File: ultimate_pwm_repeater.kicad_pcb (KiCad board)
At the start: 2 copper layers, 50.5 x 43 mm, 21 parts, among them J1 POWER, J2 SIGNAL, Q1 IRF3205, Q2 IRF3205, Q3 IRF3205, Q4 IRF3205

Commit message: added mounting holes
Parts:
- added LH: MountingHole_2.5mm_Pad, MountingHole:MountingHole_2.5mm_Pad, F.Cu at (41.5, 84.5)
- added RH: MountingHole_2.5mm_Pad, MountingHole:MountingHole_2.5mm_Pad, F.Cu at (86.0, 84.5)
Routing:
- removed copper zone on F.Cu, net GND
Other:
- board size 50.5 x 43 mm -> 50.5 x 48.5 mm
- board text added: "12-24V@20A PWM Repeater V0.3 by Hex of the River and the Sparks me@hex128.io"
- board text removed: "12-24V@20A PWM Repeater V0.2 by Hex of the River and the Sparks me@hex128.io"
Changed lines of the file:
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@@
 		(title "PWM Repeater")
 		(date "2025-04-30")
-		(rev "0.2")
+		(rev "0.3")
 		(company "Hex of the River and the Sparks")
 	)
@@
 		)
 	)
+	(footprint "MountingHole:MountingHole_2.5mm_Pad"
+		(layer "F.Cu")
+		(at 86 84.5)
+		(descr "Mounting Hole 2.5mm")
+		(tags "mounting hole 2.5mm")
+		(property "Reference" "RH"
+			(at 0 -3.5 0)
+			(layer "F.SilkS")
+			(hide yes)
+			(effects
+				(font
+					(size 1 1)
+					(thickness 0.15)
+				)
+			)
+		)
+		(property "Value" "MountingHole_2.5mm_Pad"
+			(at 0 3.5 0)
+			(layer "F.Fab")
+			(effects
+				(font
+					(size 1 1)
+					(thickness 0.15)
+				)
+			)
+		)
+		(property "Datasheet" ""
+			(at 0 0 0)
+			(unlocked yes)
+			(layer "F.Fab")
+			(hide yes)
+			(effects
+				(font
+					(size 1.27 1.27)
+					(thickness 0.15)
+				)
+			)
+		)
+		(property "Description" ""
+			(at 0 0 0)
+			(unlocked yes)
+			(layer "F.Fab")
+			(hide yes)
+			(effects
+				(font
+					(size 1.27 1.27)
+					(thickness 0.15)
+				)
+			)
+		)
+		(attr exclude_from_pos_files exclude_from_bom)
+		(fp_circle
+			(center 0 0)
+			(end 2.5 0)
+			(stroke
+				(width 0.15)
+				(type solid)
+			)
+			(fill no)
+			(layer "Cmts.User")
+		)
+		(fp_circle
+			(center 0 0)
+			(end 2.75 0)
+			(stroke
+				(width 0.05)
+				(type solid)
+			)
+			(fill no)
+			(layer "F.CrtYd")
+		)
+		(fp_text user "${REFERENCE}"
+			(at 0 0 0)
+			(layer "F.Fab")
+			(effects
+				(font
+					(size 1 1)
+					(thickness 0.15)
+				)
+			)
+		)
+		(pad "1" thru_hole circle
+			(at 0 0)
+			(size 5 5)
+			(drill 2.5)
+			(layers "*.Cu" "*.Mask")
+			(remove_unused_layers no)
+		)
+		(embedded_fonts no)
+	)
 	(footprint "PCM_Capacitor_THT_AKL:CP_Radial_D10.0mm_P2.50mm"
 		(layer "F.Cu")
@@
 		)
 	)
+	(footprint "MountingHole:MountingHole_2.5mm_Pad"
+		(layer "F.Cu")
+		(at 41.5 84.5)
+		(descr "Mounting Hole 2.5mm")
+		(tags "mounting hole 2.5mm")
+		(property "Reference" "LH"
+			(at 0 -3.5 0)
+			(layer "F.SilkS")
+			(hide yes)
+			(effects
+				(font
+					(size 1 1)
+					(thickness 0.15)
+				)
+			)
+		)
+		(property "Value" "MountingHole_2.5mm_Pad"
+			(at 0 3.5 0)
+			(layer "F.Fab")
+			(effects
+				(font
+					(size 1 1)
+					(thickness 0.15)
+				)
+			)
+		)
+		(property "Datasheet" ""
+			(at 0 0 0)
+			(unlocked yes)
+			(layer "F.Fab")
+			(hide yes)
+			(effects
+				(font
+					(size 1.27 1.27)
+					(thickness 0.15)
+				)
+			)
+		)
+		(property "Description" ""
+			(at 0 0 0)
+			(unlocked yes)
+			(layer "F.Fab")
+			(hide yes)
+			(effects
+				(font
+					(size 1.27 1.27)
+					(thickness 0.15)
+				)
+			)
+		)
+		(attr exclude_from_pos_files exclude_from_bom)
+		(fp_circle
+			(center 0 0)
+			(end 2.5 0)
+			(stroke
+				(width 0.15)
+				(type solid)
+			)
+			(fill no)
+			(layer "Cmts.User")
+		)
+		(fp_circle
+			(center 0 0)
+			(end 2.75 0)
+			(stroke
+				(width 0.05)
+				(type solid)
+			)
+			(fill no)
+			(layer "F.CrtYd")
+		)
+		(fp_text user "${REFERENCE}"
+			(at 0 0 0)
+			(layer "F.Fab")
+			(effects
+				(font
+					(size 1 1)
+					(thickness 0.15)
+				)
+			)
+		)
+		(pad "1" thru_hole circle
+			(at 0 0)
+			(size 5 5)
+			(drill 2.5)
+			(layers "*.Cu" "*.Mask")
+			(remove_unused_layers no)
+		)
+		(embedded_fonts no)
+	)
 	(footprint "PCM_Resistor_SMD_AKL:R_1206_3216Metric"
 		(layer "F.Cu")
@@
 	(gr_rect
 		(start 38.5 39)
-		(end 89 82)
+		(end 89 87.5)
 		(stroke
 			(width 0.05)
@@
 		)
 	)
-	(gr_text "12-24V@20A PWM Repeater V0.2\nby Hex of the River\nand the Sparks\nme@hex128.io"
+	(gr_text "12-24V@20A PWM Repeater V0.3\nby Hex of the River\nand the Sparks\nme@hex128.io"
 		(at 43.5 44.5 90)
 		(layer "F.SilkS")
@@
 			)
 		)
-	)
-	(zone
-		(net 1)
-		(net_name "GND")
-		(layer "F.Cu")
-		(hatch edge 0.5)
-		(priority 2)
-		(connect_pads yes
-			(clearance 0.5)
-		)
-		(min_thickness 0.5)
-		(filled_areas_thickness no)
-		(fill yes
-			(thermal_gap 0.5)
-			(thermal_bridge_width 0.5)
-			(smoothing chamfer)
-		)
-		(polygon
-			(pts
-				(xy 51 82) (xy 51 62.5) (xy 46.5 62.5) (xy 46.5 56.5) (xy 59 56.5) (xy 59 69) (xy 71.5 69) (xy 71.5 75)
-				(xy 44 75) (xy 44 82) (xy 88.5 82) (xy 88.5 62) (xy 88.5 39) (xy 39 39) (xy 39 82)
-			)
-		)

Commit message: re-added the top gnd fill zone (introduced in 0.3)
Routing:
- added copper zone on F.Cu, net GND
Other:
- board text added: "12-24V@20A PWM Repeater V0.4 by Hex of the River and the Sparks me@hex128.io"
- board text removed: "12-24V@20A PWM Repeater V0.3 by Hex of the River and the Sparks me@hex128.io"
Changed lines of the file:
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@@
 		(title "PWM Repeater")
 		(date "2025-04-30")
-		(rev "0.3")
+		(rev "0.4")
 		(company "Hex of the River and the Sparks")
 	)
@@
 		)
 	)
-	(gr_text "12-24V@20A PWM Repeater V0.3\nby Hex of the River\nand the Sparks\nme@hex128.io"
+	(gr_text "12-24V@20A PWM Repeater V0.4\nby Hex of the River\nand the Sparks\nme@hex128.io"
 		(at 43.5 44.5 90)
 		(layer "F.SilkS")
@@
 	)
 	(zone
+		(net 1)
+		(net_name "GND")
+		(layer "F.Cu")
+		(hatch edge 0.5)
+		(priority 2)
+		(connect_pads yes
+			(clearance 0.5)
+		)
+		(min_thickness 0.5)
+		(filled_areas_thickness no)
+		(fill yes
+			(thermal_gap 0.5)
+			(thermal_bridge_width 0.5)
+			(smoothing chamfer)
+			(radius 0.5)
+		)
+		(polygon
+			(pts
+				(xy 39.5 39) (xy 88 39) (xy 88 80.5) (xy 71.5 80.5) (xy 71.5 69) (xy 59 69) (xy 59 56.5) (xy 46.5 56.5)
+				(xy 46.5 62.5) (xy 51 62.5) (xy 51 75) (xy 72 75) (xy 72 80.5) (xy 39.5 80.5)
+			)
+		)
+	)
+	(zone
 		(net 6)
 		(net_name "+24V")
@@
 			(thermal_bridge_width 0.5)
 			(smoothing chamfer)
+			(radius 0.5)
 		)
 		(polygon
@@
 			(thermal_gap 0.5)
 			(thermal_bridge_width 0.5)
+			(smoothing chamfer)
+			(radius 0.5)
 			(island_removal_mode 1)
 			(island_area_min 10)
@@
 		(polygon
 			(pts
-				(xy 39.5 39) (xy 39.5 82) (xy 88 82) (xy 88 39)
+				(xy 39.5 39) (xy 39.5 80.5) (xy 88 80.5) (xy 88 39)
 			)
 		)

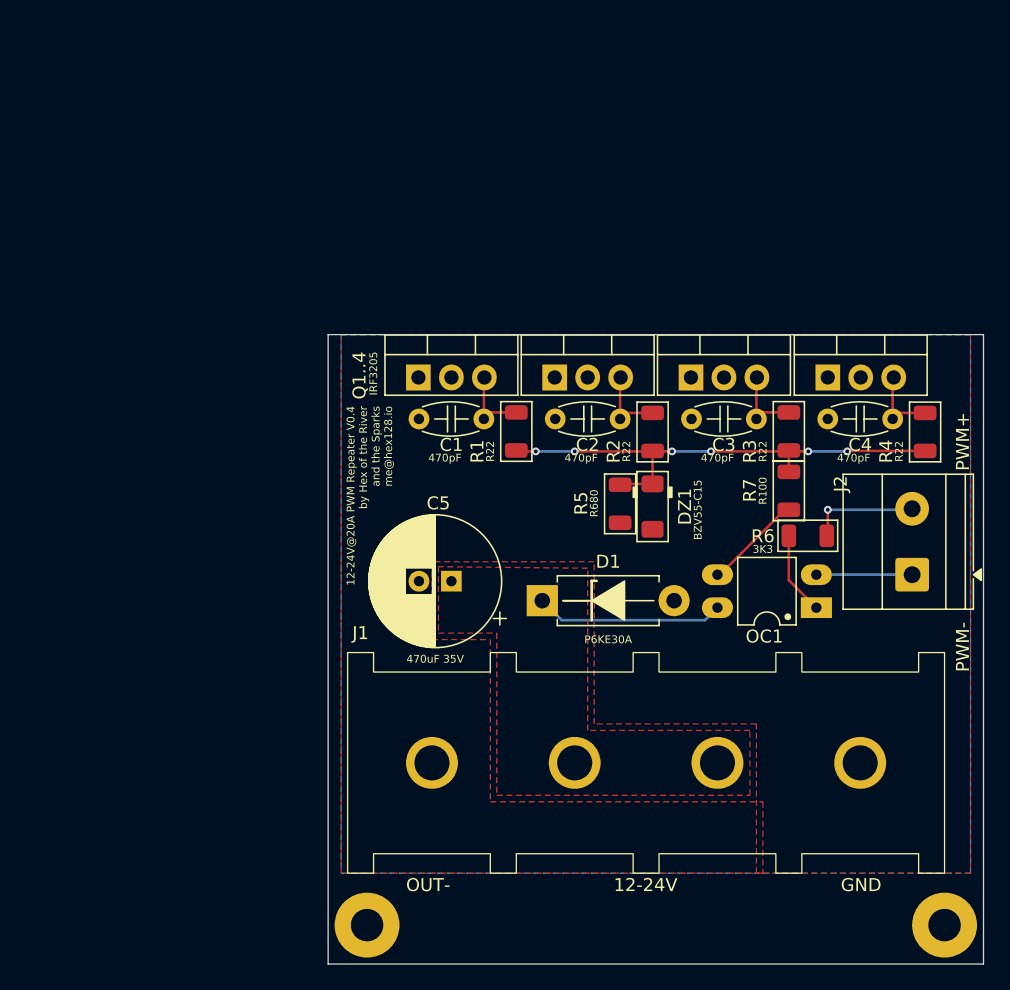
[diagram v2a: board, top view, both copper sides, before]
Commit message: fixed reverse mosfet connection, rearranged pcb
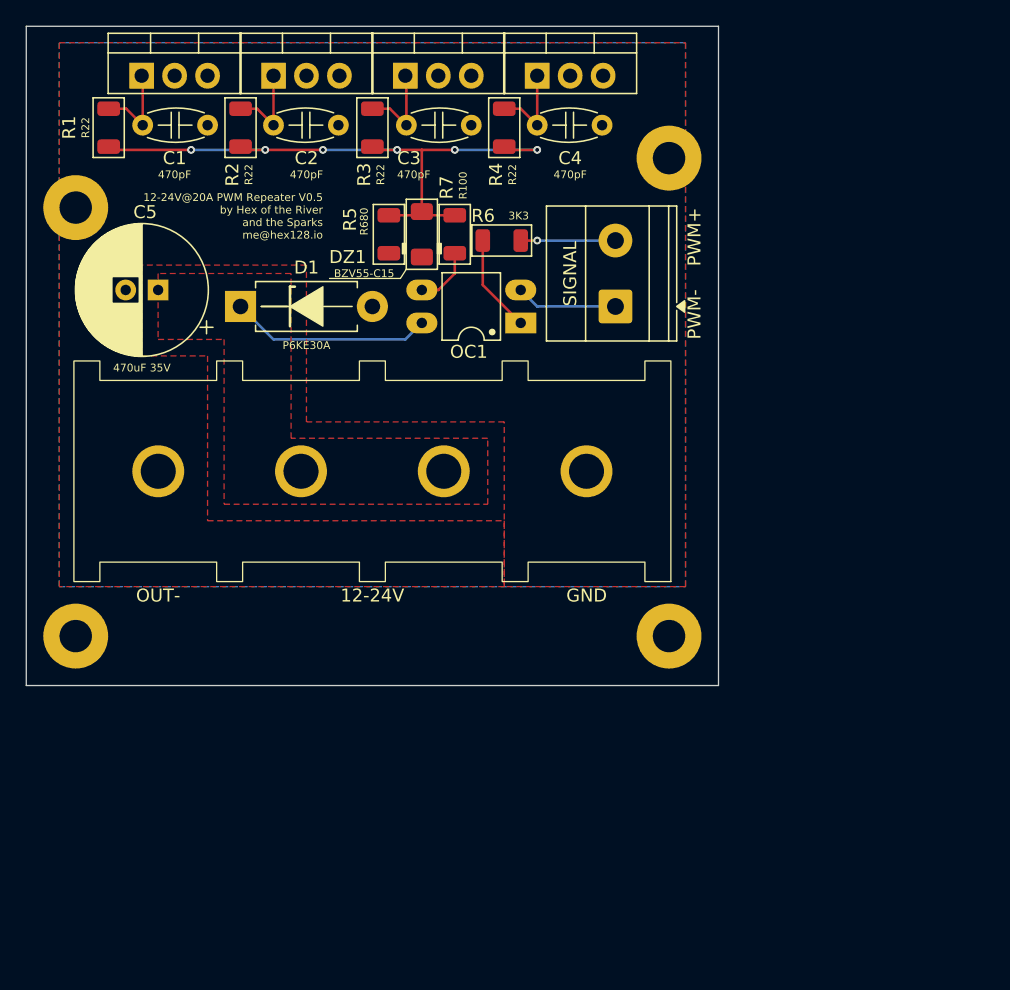
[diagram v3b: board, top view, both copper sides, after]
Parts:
- added LTH: MountingHole_2.5mm_Pad, MountingHole:MountingHole_2.5mm_Pad, F.Cu at (19.1, 29.2)
- added RTH: MountingHole_2.5mm_Pad, MountingHole:MountingHole_2.5mm_Pad, F.Cu at (64.8, 25.4)
- moved R4 40.0 mm to (52.1, 23.1), turned to 90 degrees
- moved R3 39.7 mm to (41.9, 23.1), turned to 90 degrees
- moved R2 39.5 mm to (31.8, 23.1), turned to 90 degrees
- moved R1 39.2 mm to (21.6, 23.1), turned to 90 degrees
- moved R6 32.8 mm to (51.9, 31.8)
- moved D1 32.5 mm to (31.8, 36.8)
- moved R7 32.5 mm to (48.3, 31.3)
- moved Q4 32.3 mm to (54.6, 19.1)
- moved Q3 32.0 mm to (44.5, 19.1)
- moved C5 31.8 mm to (25.4, 35.6)
- moved C4 31.8 mm to (54.6, 22.9)
- moved Q2 31.8 mm to (34.3, 19.1)
- moved OC1 31.6 mm to (53.3, 38.1)
- moved LH 31.6 mm to (19.1, 62.2)
- moved Q1 31.6 mm to (24.1, 19.1)
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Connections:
- C1 pad 2: Net-(Q1-S) -> Net-(Q1-G)
- C2 pad 1: GND -> Net-(Q2-G)
- C2 pad 2: Net-(Q2-S) -> GND
- C3 pad 2: Net-(Q3-S) -> Net-(Q3-G)
- C4 pad 1: GND -> Net-(Q4-G)
- C4 pad 2: Net-(Q4-S) -> GND
- DZ1 pad 1: Net-(DZ1-K) -> GND
- DZ1 pad 2: GND -> Net-(DZ1-A)
- Q1 pad 1: GND -> Net-(Q1-G)
- Q1 pad 3: Net-(Q1-S) -> GND
- Q2 pad 1: GND -> Net-(Q2-G)
- Q2 pad 3: Net-(Q2-S) -> GND
- Q3 pad 1: GND -> Net-(Q3-G)
- Q3 pad 3: Net-(Q3-S) -> GND
- Q4 pad 1: GND -> Net-(Q4-G)
- Q4 pad 3: Net-(Q4-S) -> GND
- R1 pad 1: Net-(Q1-S) -> Net-(DZ1-A)
- R1 pad 2: Net-(DZ1-K) -> Net-(Q1-G)
- R2 pad 1: Net-(Q2-S) -> Net-(DZ1-A)
- R2 pad 2: Net-(DZ1-K) -> Net-(Q2-G)
- R3 pad 1: Net-(Q3-S) -> Net-(DZ1-A)
- R3 pad 2: Net-(DZ1-K) -> Net-(Q3-G)
- R4 pad 1: Net-(Q4-S) -> Net-(DZ1-A)
- R4 pad 2: Net-(DZ1-K) -> Net-(Q4-G)
- R5 pad 2: Net-(DZ1-K) -> Net-(DZ1-A)
- R7 pad 1: Net-(DZ1-K) -> Net-(DZ1-A)
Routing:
- net Net-(DZ1-A): track 0.00 -> 49.9 mm, vias 0 -> 6
- net Net-(DZ1-K): track 38.4 -> 0.00 mm, vias 6 -> 0
- net Net-(Q3-G): track 0.00 -> 6.99 mm
- net Net-(Q1-G): track 0.00 -> 6.99 mm
- net Net-(Q4-G): track 0.00 -> 6.88 mm
- net Net-(Q2-G): track 0.00 -> 6.88 mm
- net Net-(Q3-S): track 5.98 -> 0.00 mm
- net Net-(Q4-S): track 5.92 -> 0.00 mm
- net Net-(Q1-S): track 5.92 -> 0.00 mm
- net Net-(Q2-S): track 5.91 -> 0.00 mm
- net Net-(OC1-Pad3): track 7.70 -> 4.62 mm
- net Net-(OC1-Pad1): track 6.42 -> 7.56 mm
- net +24V: track 14.5 -> 15.5 mm
- net PWM-: track 6.88 -> 7.83 mm
- net PWM+: track 8.03 -> 7.30 mm
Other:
- board size 50.5 x 48.5 mm -> 53.3 x 50.8 mm
- board text added: "12-24V@20A PWM Repeater V0.5 by Hex of the River and the Sparks me@hex128.io"
- board text removed: "12-24V@20A PWM Repeater V0.4 by Hex of the River and the Sparks me@hex128.io"
- board text removed: "Q1..4"

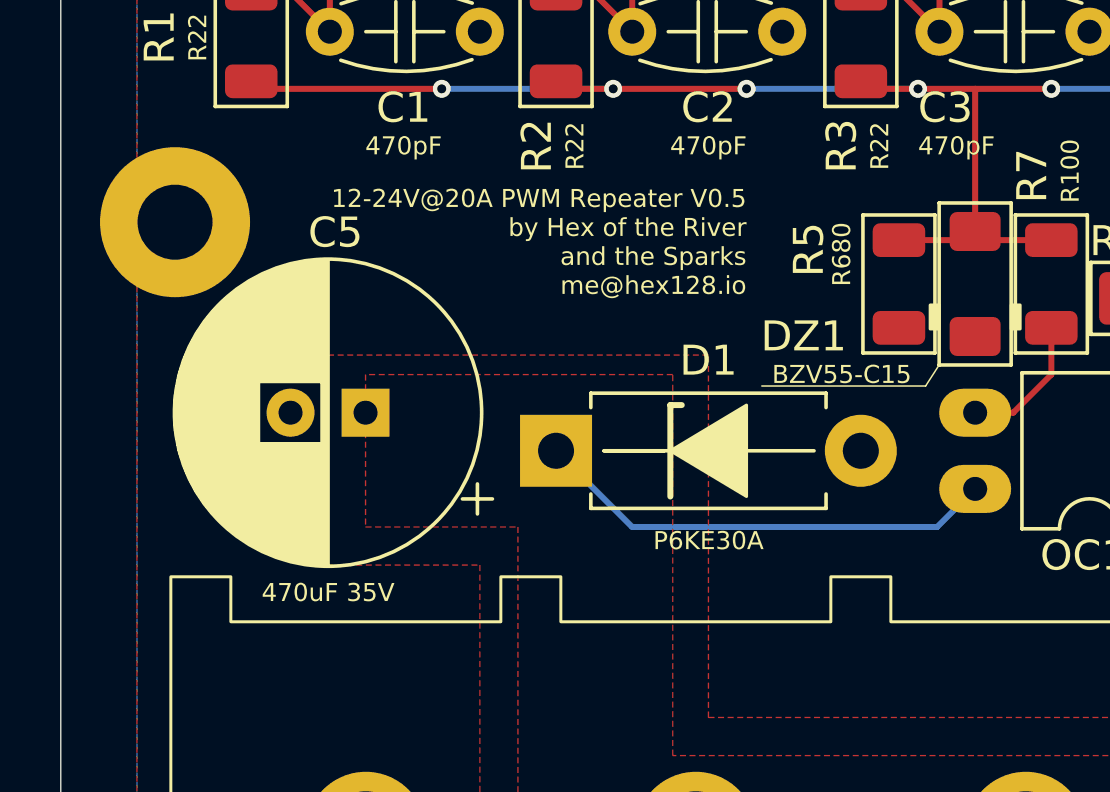
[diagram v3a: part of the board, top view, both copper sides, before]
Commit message: 18v zener, 3.5mm pitch capacitor
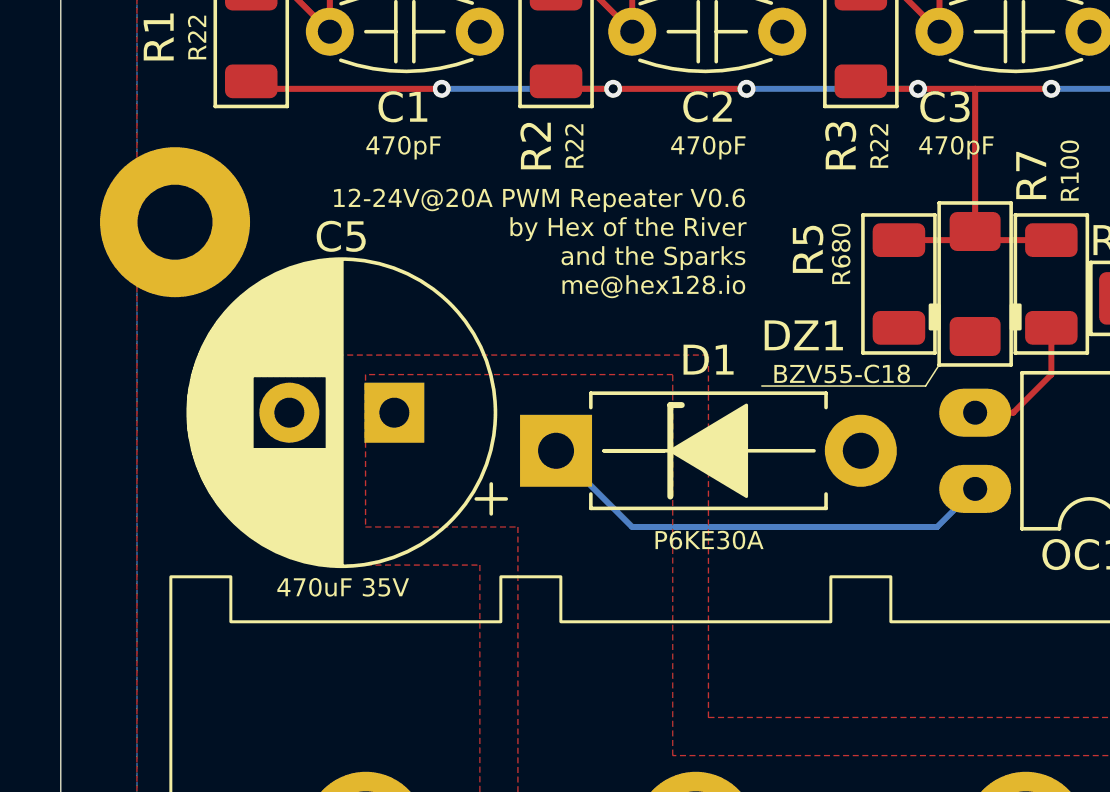
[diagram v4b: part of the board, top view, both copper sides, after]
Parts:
- C5: footprint PCM_Capacitor_THT_AKL:CP_Radial_D10.0mm_P2.50mm -> Capacitor_THT:CP_Radial_D10.0mm_P3.50mm
- DZ1: value BZV55-C15 -> BZV55-C18
- moved C5 0.96 mm to (26.4, 35.6)
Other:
- board text added: "12-24V@20A PWM Repeater V0.6 by Hex of the River and the Sparks me@hex128.io"
- board text removed: "12-24V@20A PWM Repeater V0.5 by Hex of the River and the Sparks me@hex128.io"
